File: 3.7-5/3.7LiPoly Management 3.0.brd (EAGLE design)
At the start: 25 x 55 mm, 32 parts, among them J1 DX4R005HJ5R2000, J2 S2B-PH-SM4-TB(LF)(SN), T1 MMUN2133LT1G, U1 TPS61090RSAR, U2 MCP73871T-2CCI/ML

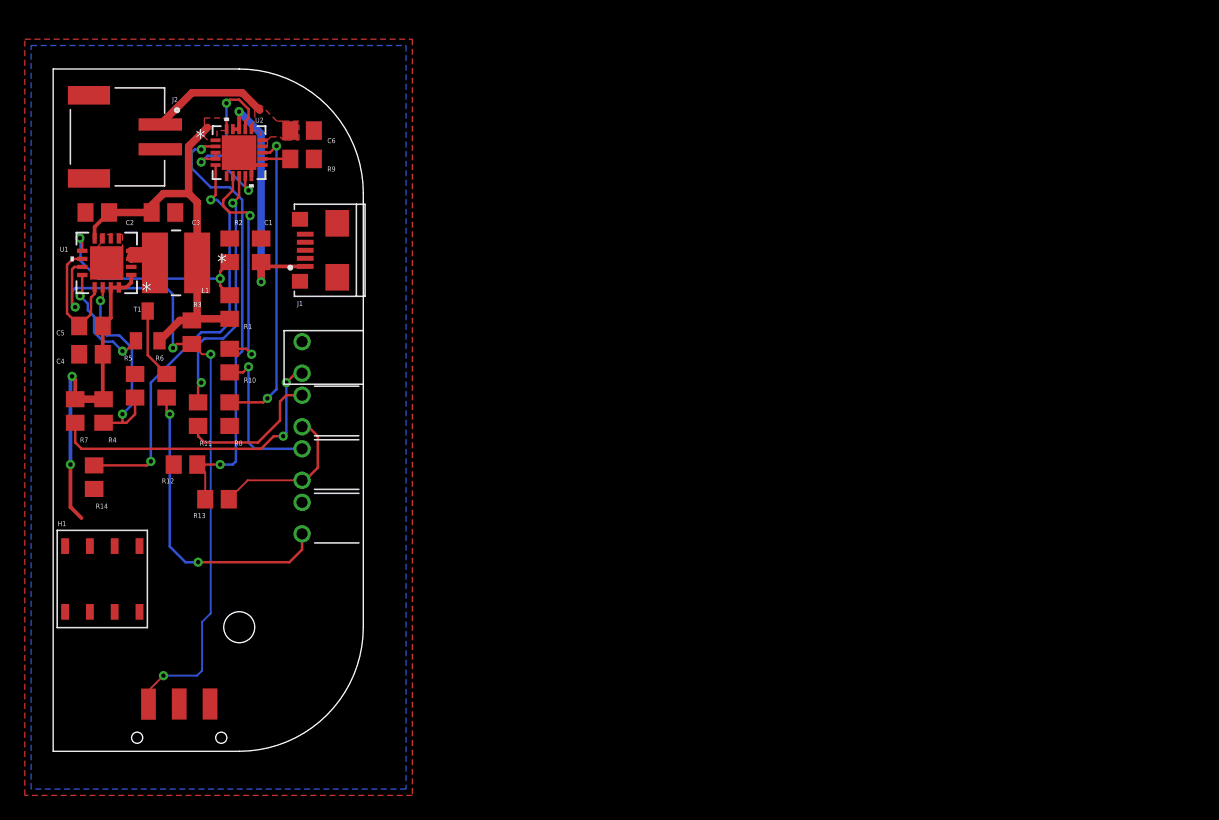
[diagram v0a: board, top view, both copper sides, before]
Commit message: Update
Moved shoulder buttons to LiPoly Management and extended LiPoly Management's dimensions. After looking at the boards in Fusion 360, I decided it would be better to have the shoulder buttons lower, rather than up high on RPi Zero Breakout. Rereouted LiPoly due to this.
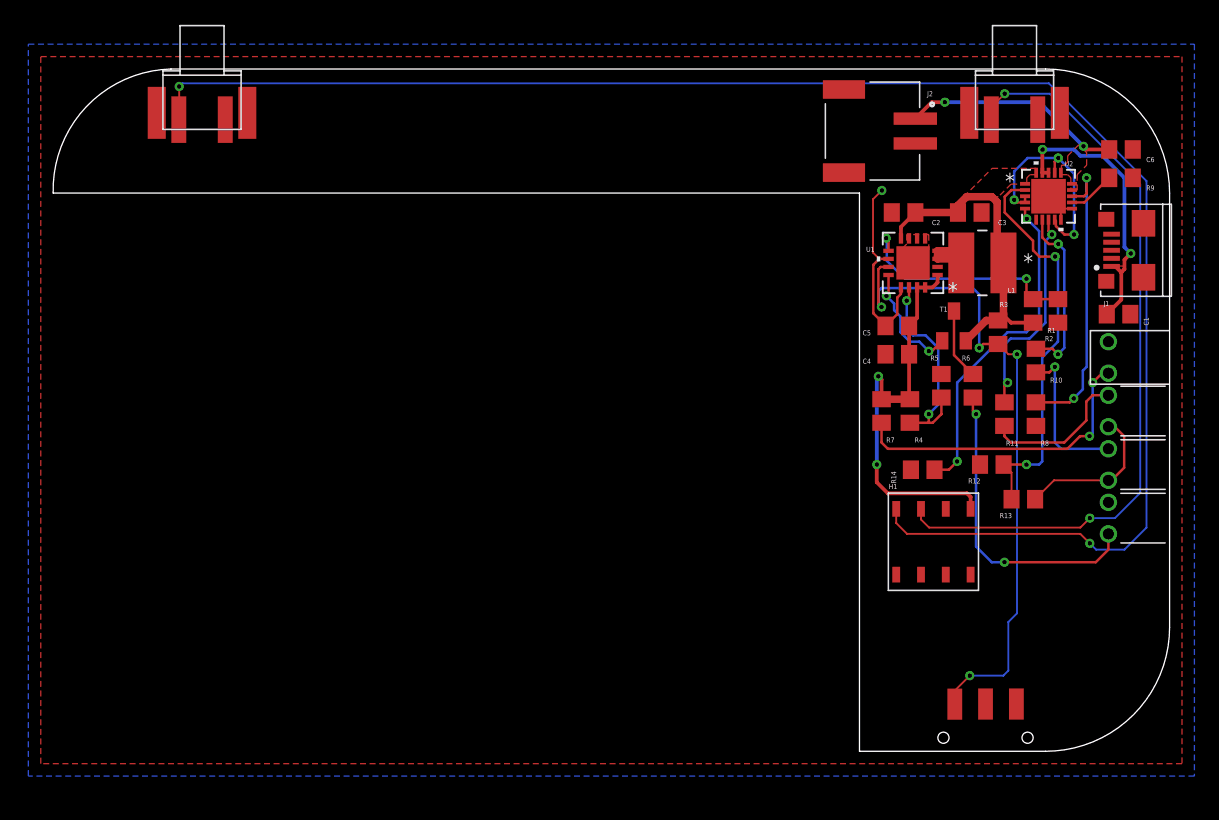
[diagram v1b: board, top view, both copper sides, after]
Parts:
- added U$1, U$3: SPST_TACTILE_SWITCHRIGHTANGLEBENT, switches:SPST_TACTILESWITCH_TL3360CF185Q_BENTFRAME
- moved C1 69.3 mm to (85.9, 35.2), turned to 0 degrees
- moved H1 67.1 mm to (71.4, 17.0)
- moved R2 67.0 mm to (81.0, 35.5), turned to 90 degrees
- moved R14 66.8 mm to (70.1, 22.7), turned to 0 degrees
- moved C6 66.0 mm to (86.1, 48.5)
- moved R9 66.0 mm to (86.1, 46.2)
- moved U2 65.3 mm to (80.2, 44.7)
- moved C2 65.0 mm to (68.6, 43.4)
- moved C3 65.0 mm to (73.9, 43.4)
- moved C4 65.0 mm to (68.0, 32.0)
- moved C5 65.0 mm to (68.0, 34.3)
- moved CHARGE 65.0 mm to (85.1, 27.4)
- moved DONE 65.0 mm to (85.1, 23.1)
- moved J1 65.0 mm to (85.3, 40.4)
- moved L1 65.0 mm to (74.9, 39.4)
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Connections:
- new net N$10: H1.P4, U$1.P$1
- new net N$15: H1.P3, U$3.P$1
- net GND: now also U$1.P$2, U$3.P$2
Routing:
- net N$10: track 0.00 -> 134.9 mm, vias 0 -> 2
- net N$15: track 0.00 -> 61.3 mm, vias 0 -> 2
- net VLIPO: track 9.65 -> 17.8 mm, vias 0 -> 2
- net VBAT: track 33.6 -> 26.1 mm
- net N$13: track 33.2 -> 26.6 mm
- net GND: track 13.6 -> 20.1 mm, vias 0 -> 1
- net VOUT: track 27.8 -> 33.6 mm
- net N$12: track 18.5 -> 14.2 mm
- net N$14: track 36.1 -> 32.5 mm
- net N$11: track 20.9 -> 17.5 mm
- net N$8: track 2.24 -> 3.83 mm
- net N$4: track 25.2 -> 23.9 mm
- net CTRL: track 16.9 -> 18.1 mm
- net VBUS: track 22.2 -> 22.9 mm
- net N$1: track 18.1 -> 18.7 mm
- added copper zone on layer 1, net VBUS
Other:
- board size 25 x 55 mm -> 90 x 55 mm
- board text added: "3.7-5V LiPoly Management Rev 3 2019 Injoo Moon"
- board text removed: "3.7-5V LiPoly Management Rev 2 2019 Injoo Moon"
